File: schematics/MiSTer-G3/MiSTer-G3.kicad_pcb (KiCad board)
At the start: 2 copper layers, 130 x 91.5 mm, 37 parts, among them J1 Apple J20, J2 VGA Input, J3 Audio, J4 I2S, J5 Power, J6 Rotary Encoder, U1 TPA6021A4N, U2 UDA1334A, U3 LCC110

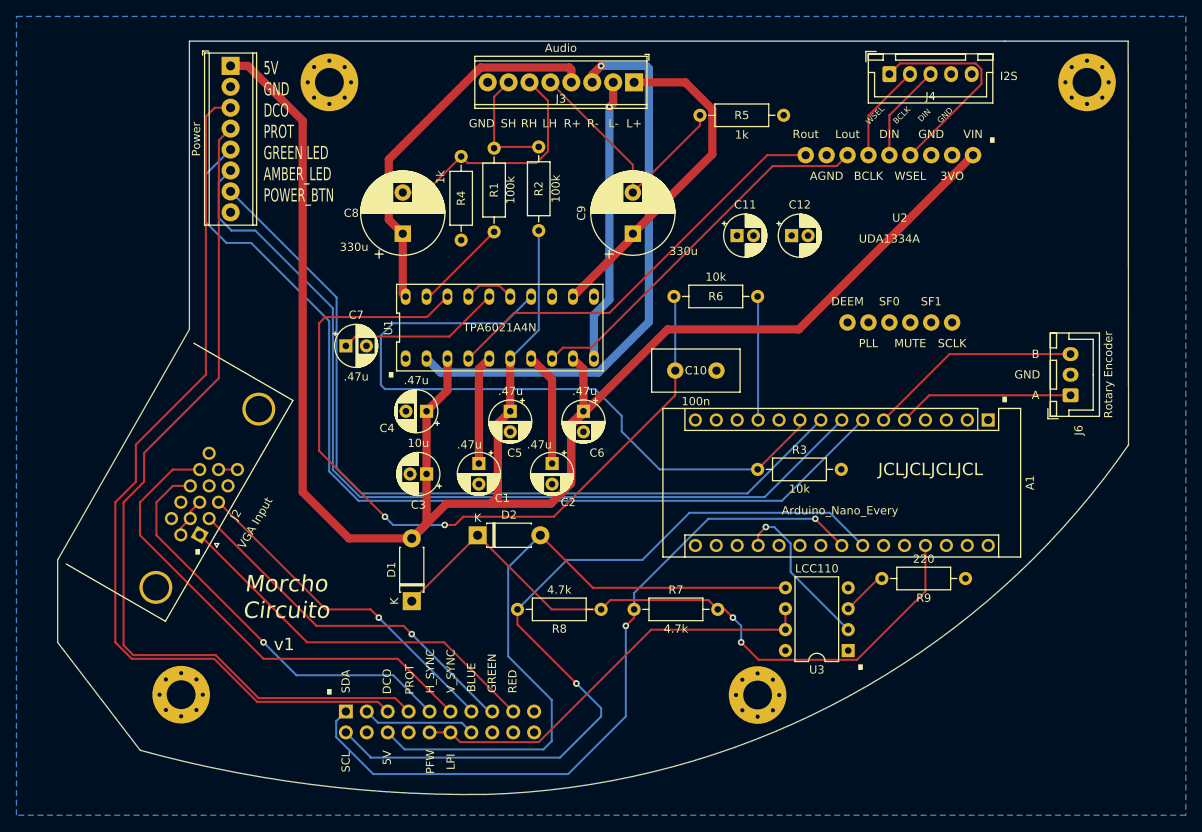
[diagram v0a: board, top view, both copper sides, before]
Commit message: Headers and routing
Added JST header for mister buttons
Split screw terminals into separate JST headers for speakers, headphones and front panel.
Added rotary encoder button

Re-routed pcb
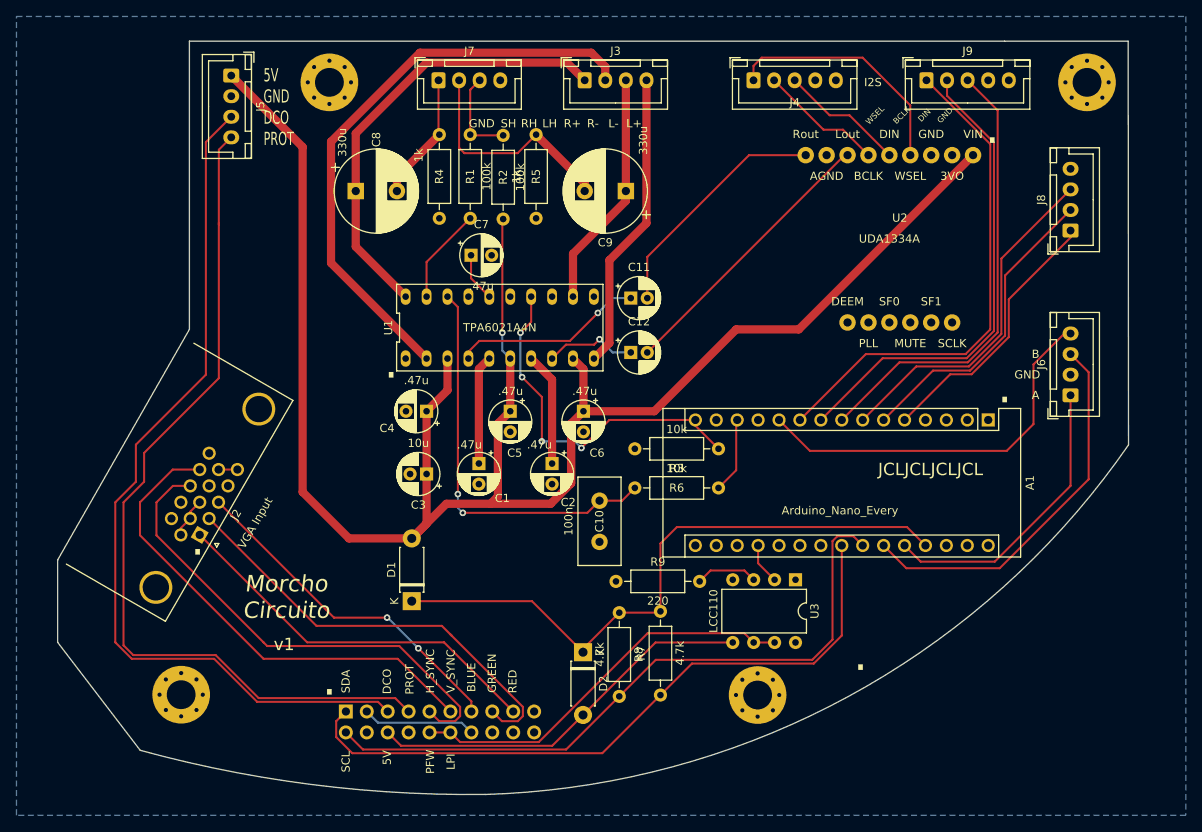
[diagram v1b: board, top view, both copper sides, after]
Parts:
- added J7: Headphones, Connector_JST:JST_XH_B4B-XH-A_1x04_P2.50mm_Vertical, F.Cu at (122.2, 51.8)
- added J8: Front Panel, Connector_JST:JST_XH_B4B-XH-A_1x04_P2.50mm_Vertical, F.Cu at (199.0, 70.0)
- added J9: Buttons, Connector_JST:JST_XH_B5B-XH-A_1x05_P2.50mm_Vertical, F.Cu at (181.5, 51.8)
- J3: value Audio -> Speaker; footprint TerminalBlock_Phoenix:TerminalBlock_Phoenix_MPT-0,5-8-2.54_1x08_P2.54mm_Horizontal -> Connector_JST:JST_XH_B4B-XH-A_1x04_P2.50mm_Vertical
- J5: footprint TerminalBlock_Phoenix:TerminalBlock_Phoenix_MPT-0,5-8-2.54_1x08_P2.54mm_Horizontal -> Connector_JST:JST_XH_B4B-XH-A_1x04_P2.50mm_Vertical
- J6: footprint Connector_JST:JST_XH_B3B-XH-A_1x03_P2.50mm_Vertical -> Connector_JST:JST_XH_B4B-XH-A_1x04_P2.50mm_Vertical
- moved R9 42.5 mm to (143.8, 112.6), turned to 0 degrees
- moved C12 24.1 mm to (145.6, 84.8)
- moved R6 23.7 mm to (156.2, 101.2)
- moved R5 20.0 mm to (134.1, 58.4), turned to 270 degrees
- moved D2 19.1 mm to (139.8, 121.2), turned to 270 degrees
- moved C7 18.8 mm to (126.2, 73.0)
- moved C10 18.3 mm to (141.8, 102.8), turned to 270 degrees
- moved J4 16.5 mm to (160.5, 51.8)
- moved C11 15.0 mm to (145.6, 78.2)
- moved R7 10.9 mm to (149.2, 126.4), turned to 90 degrees
- moved U3 10.7 mm to (165.6, 112.4), turned to 270 degrees
- moved C8 7.71 mm to (112.2, 65.2), turned to 0 degrees
- moved J3 6.01 mm to (140.0, 51.8), turned to 0 degrees
- moved R3 5.37 mm to (156.2, 96.5), turned to 180 degrees
- moved C9 5.25 mm to (145.0, 65.2), turned to 180 degrees
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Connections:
- A1 pad 10: AMP_ACTIVE -> BTN_USER
- A1 pad 11: Net-(A1-Pad11) -> ROT_BTN
- A1 pad 15: Net-(A1-Pad15) -> AMP_ACTIVE
- A1 pad 25: Net-(A1-Pad25) -> ROT_B
- A1 pad 26: Net-(A1-Pad26) -> ROT_A
- A1 pad 5: ROT_A -> GREEN_LED
- A1 pad 6: ROT_B -> AMBER_LED
- A1 pad 7: GREEN_LED -> POWER_BTN
- A1 pad 8: AMBER_LED -> BTN_RESET
- A1 pad 9: POWER_BTN -> BTN_OSD
- J3 pad 1: LSPKR+ -> RSPKR+
- J3 pad 2: LSPKR- -> RSPKR-
- J3 pad 3: RSPKR- -> LSPKR+
- J3 pad 4: RSPKR+ -> LSPKR-
- R6 pad 1: Net-(A1-Pad12) -> Net-(A1-Pad13)
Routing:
- net GREEN_LED: track 118.6 -> 32.9 mm
- net AMBER_LED: track 111.4 -> 37.5 mm
- net BTN_USER: track 0.00 -> 61.1 mm
- net POWER_BTN: track 102.7 -> 42.2 mm
- net BTN_OSD: track 0.00 -> 58.3 mm
- net BTN_RESET: track 0.00 -> 55.5 mm
- net VOLUME: track 98.2 -> 49.2 mm
- net ROT_BTN: track 0.00 -> 47.1 mm
- net AMP_ACTIVE: track 85.4 -> 44.2 mm, vias 0 -> 4
- net 5V_TRICKLE: track 82.4 -> 47.8 mm
- net Net-(C11-Pad1): track 0.00 -> 23.2 mm, vias 0 -> 1
- net RIN: track 51.2 -> 29.4 mm
- net ROT_B: track 26.0 -> 46.6 mm
- net IVAD_SCL: track 100.0 -> 81.8 mm, vias 1 -> 0
- net Net-(A1-Pad12): track 15.1 -> 0.00 mm
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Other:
- board text added: "5V GND DCO PROT"
- board text removed: "5V GND DCO PROT GREEN LED AMBER_LED POWER_BTN"

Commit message: Headphone sense
Added second sense wire from j22 board since they can't be combined.
Send sense inputs to arduino and control SE/~BTL signal from there. This will allow different volume settings for each mode.
Re-route.
Fix silkscreen labels
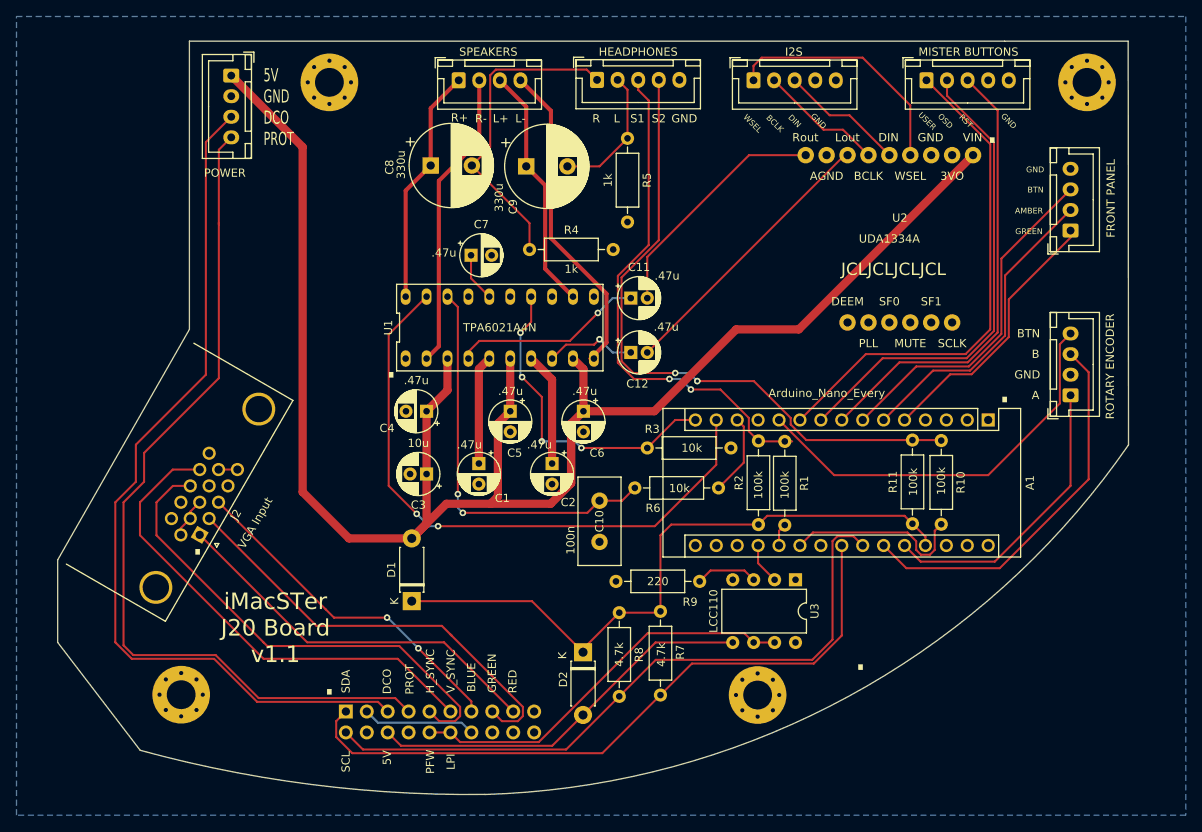
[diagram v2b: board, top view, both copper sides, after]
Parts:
- added R10: 100k, Resistor_THT:R_Axial_DIN0207_L6.3mm_D2.5mm_P10.16mm_Horizontal, F.Cu at (183.3, 95.5)
- added R11: 100k, Resistor_THT:R_Axial_DIN0207_L6.3mm_D2.5mm_P10.16mm_Horizontal, F.Cu at (179.8, 105.6)
- FRONT PANEL: renamed from J8
- HEADPHONES: renamed from J7; footprint Connector_JST:JST_XH_B4B-XH-A_1x04_P2.50mm_Vertical -> Connector_JST:JST_XH_B5B-XH-A_1x05_P2.50mm_Vertical
- MISTER BUTTONS: renamed from J9
- ROTARY ENCODER: renamed from J6
- moved R1 53.4 mm to (164.3, 95.6)
- moved R2 48.3 mm to (161.1, 105.7)
- moved HEADPHONES 19.3 mm to (141.5, 51.7)
- moved R4 17.7 mm to (133.3, 72.3), turned to 0 degrees
- moved SPEAKERS 15.3 mm to (124.7, 51.8)
- moved C9 12.5 mm to (132.9, 62.2), turned to 0 degrees
- moved R5 11.1 mm to (145.2, 58.8)
- moved C8 9.61 mm to (121.3, 62.1)
- moved R3 8.65 mm to (147.6, 96.4), turned to 0 degrees
- renumbered J5 to POWER, J3 to SPEAKERS
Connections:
- net SHEAD renamed SHEAD1
- A1 pad 1: Net-(A1-Pad1) -> (no net)
- A1 pad 12: Net-(A1-Pad12) -> (no net)
- A1 pad 14: Net-(A1-Pad14) -> AMP_SE
- A1 pad 16: Net-(A1-Pad16) -> (no net)
- A1 pad 17: Net-(A1-Pad17) -> (no net)
- A1 pad 18: Net-(A1-Pad18) -> (no net)
- A1 pad 2: Net-(A1-Pad2) -> (no net)
- A1 pad 20: Net-(A1-Pad20) -> ~HEAD_DETECT1
- A1 pad 21: Net-(A1-Pad21) -> ~HEAD_DETECT2
- A1 pad 22: Net-(A1-Pad22) -> (no net)
- A1 pad 28: Net-(A1-Pad28) -> (no net)
- A1 pad 3: Net-(A1-Pad3) -> (no net)
- A1 pad 30: Net-(A1-Pad30) -> (no net)
- HEADPHONES pad 4: GND -> SHEAD2
- J1 pad 19: Net-(J1-Pad19) -> (no net)
- J1 pad 8: Net-(J1-Pad8) -> (no net)
- J2 pad 11: Net-(J2-Pad11) -> (no net)
- J2 pad 12: Net-(J2-Pad12) -> (no net)
- J2 pad 15: Net-(J2-Pad15) -> (no net)
- J2 pad 4: Net-(J2-Pad4) -> (no net)
- J2 pad 9: Net-(J2-Pad9) -> (no net)
- J4 pad 5: Net-(J4-Pad5) -> (no net)
- MISTER BUTTONS pad 4: Net-(J9-Pad4) -> (no net)
- R1 pad 2: Net-(R1-Pad2) -> ~HEAD_DETECT1
- R2 pad 1: 5V_PSU -> 5V_MCU
- U1 pad 13: Net-(U1-Pad13) -> (no net)
- U1 pad 19: Net-(R1-Pad2) -> AMP_SE
- U2 pad 12: Net-(U2-Pad12) -> (no net)
- U2 pad 13: Net-(U2-Pad13) -> (no net)
- U2 pad 14: Net-(U2-Pad14) -> (no net)
- U2 pad 15: Net-(U2-Pad15) -> (no net)
- U2 pad 16: Net-(U2-Pad16) -> (no net)
- U2 pad 17: Net-(U2-Pad17) -> (no net)
- U2 pad 2: Net-(U2-Pad2) -> (no net)
- U3 pad 1: Net-(U3-Pad1) -> (no net)
- U3 pad 4: Net-(U3-Pad4) -> (no net)
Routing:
- net SHEAD2: track 0.00 -> 79.3 mm, vias 0 -> 2
- net AMP_SE: track 0.00 -> 75.8 mm, vias 0 -> 2
- net SHEAD1: track 11.1 -> 62.5 mm, vias 0 -> 2
- net RSPKR-: track 71.3 -> 36.4 mm
- net RSPKR+: track 54.6 -> 28.9 mm
- net RHEAD: track 15.6 -> 38.8 mm
- net ~HEAD_DETECT2: track 0.00 -> 22.4 mm
- net 5V_PSU: track 235.0 -> 217.6 mm, vias 1 -> 0
- net Net-(R1-Pad2): track 12.0 -> 0.00 mm
- net LHEAD: track 28.0 -> 16.3 mm
- net AMP_ACTIVE: track 44.2 -> 40.3 mm
- net LSPKR-: track 36.4 -> 39.3 mm
- net ~HEAD_DETECT1: track 0.00 -> 2.77 mm
- net ROT_BTN: track 47.1 -> 49.5 mm
- net 5V_MCU: track 77.2 -> 79.6 mm
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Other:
- board text added: "AMBER"
- board text added: "BTN"
- board text added: "L"
- board text added: "OSD"
- board text added: "R"
- board text added: "RST"
- board text added: "S1"
- board text added: "S2"
- board text added: "USER"
- board text added: "iMacSTer J20 Board v1.1"
- board text removed: "LH"
- board text removed: "Morcho Circuito"
- board text removed: "RH"
- board text removed: "SH"
- board text removed: "v1"

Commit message: Code and schematic changes
Fixed incorrect routing for decoupling caps
Updated code to handle headphones, power button and mister buttons.
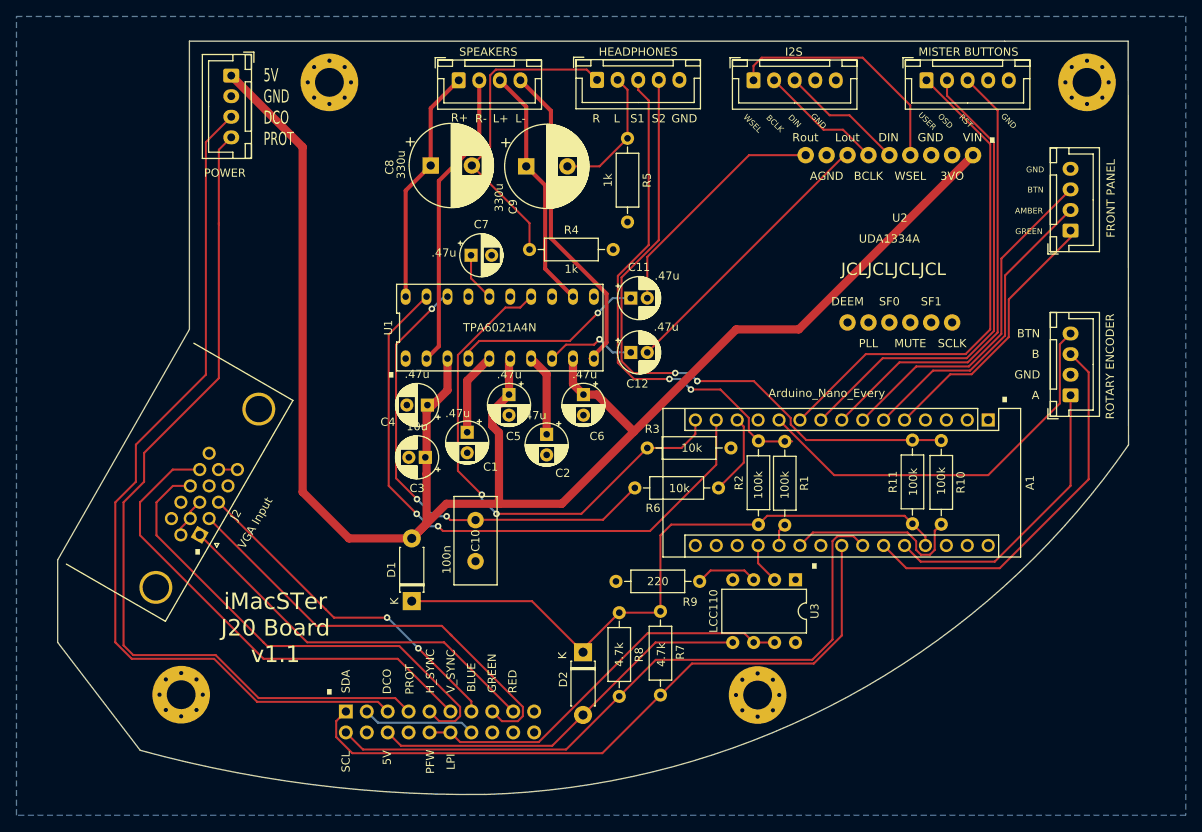
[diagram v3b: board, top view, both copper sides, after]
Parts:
- moved C10 15.2 mm to (126.7, 105.2)
- moved C1 4.06 mm to (125.7, 94.5)
- moved C2 3.61 mm to (135.4, 94.7)
- moved C5 2.03 mm to (130.8, 89.9)
- moved C3 2.03 mm to (120.7, 97.5)
- moved C6 2.02 mm to (139.8, 89.9)
- moved C4 0.76 mm to (120.9, 91.2)
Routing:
- net AMP_ACTIVE: track 40.3 -> 62.9 mm, vias 4 -> 2
- net VOLUME: track 49.2 -> 57.6 mm, vias 2 -> 3
- net 5V_PSU: track 217.6 -> 212.6 mm
- net Net-(C2-Pad1): track 13.8 -> 9.98 mm
- net Net-(C1-Pad1): track 13.3 -> 10.1 mm

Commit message: Gerber Files
Exported gerber files for all PCBs
Updated main board to version 1.2 with fixes the routing that were bodged into previous version.
Updated to kicad 6
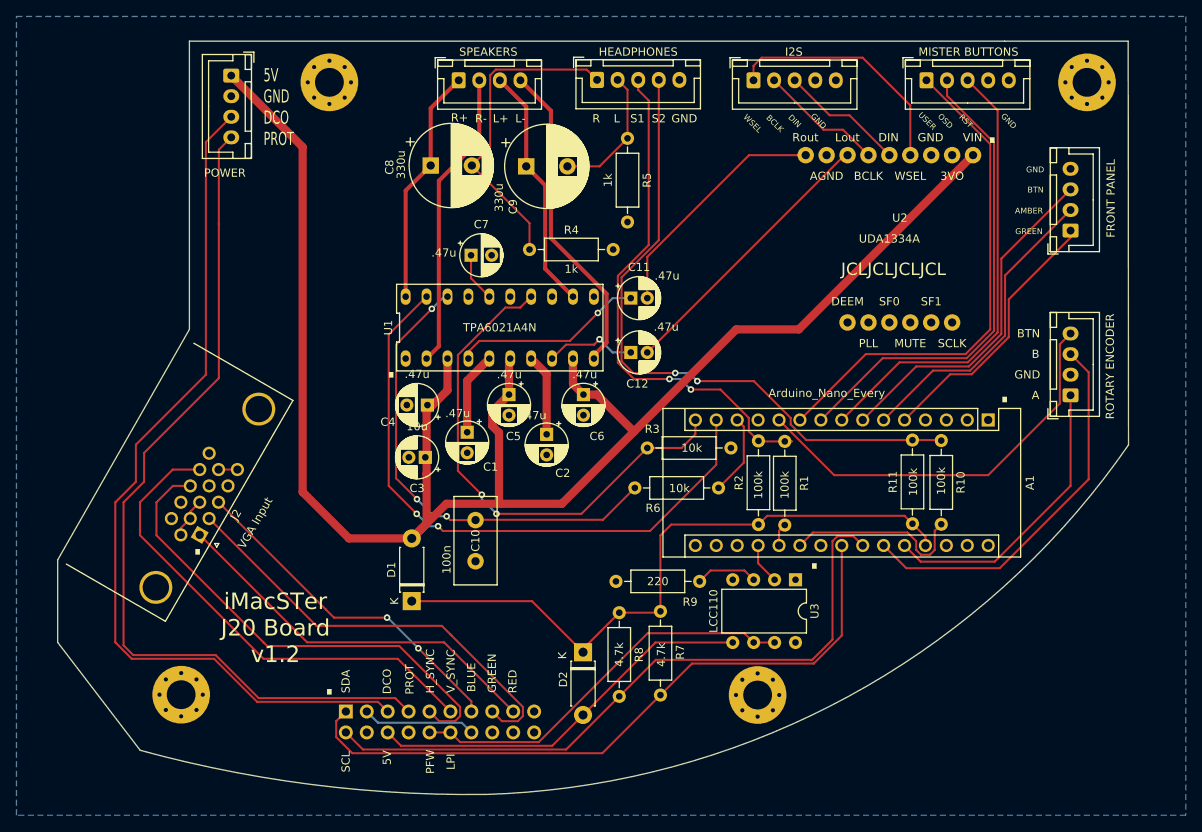
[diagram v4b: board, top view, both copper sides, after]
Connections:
- net ~HEAD_DETECT1 renamed ~{HEAD_DETECT1}
- net ~HEAD_DETECT2 renamed ~{HEAD_DETECT2}
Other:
- net class Default removed
- board text added: "iMacSTer J20 Board v1.2"
- board text removed: "iMacSTer J20 Board v1.1"
